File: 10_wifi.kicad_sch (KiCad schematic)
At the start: 25 parts, among them J1 Conn_01x03, J16 Conn_01x04, J30 Conn_01x04, J31 TYPE-C-31-M-12, J32 Conn_01x03, J33 EnUSB, U12 TLV62130, U13 FC41D

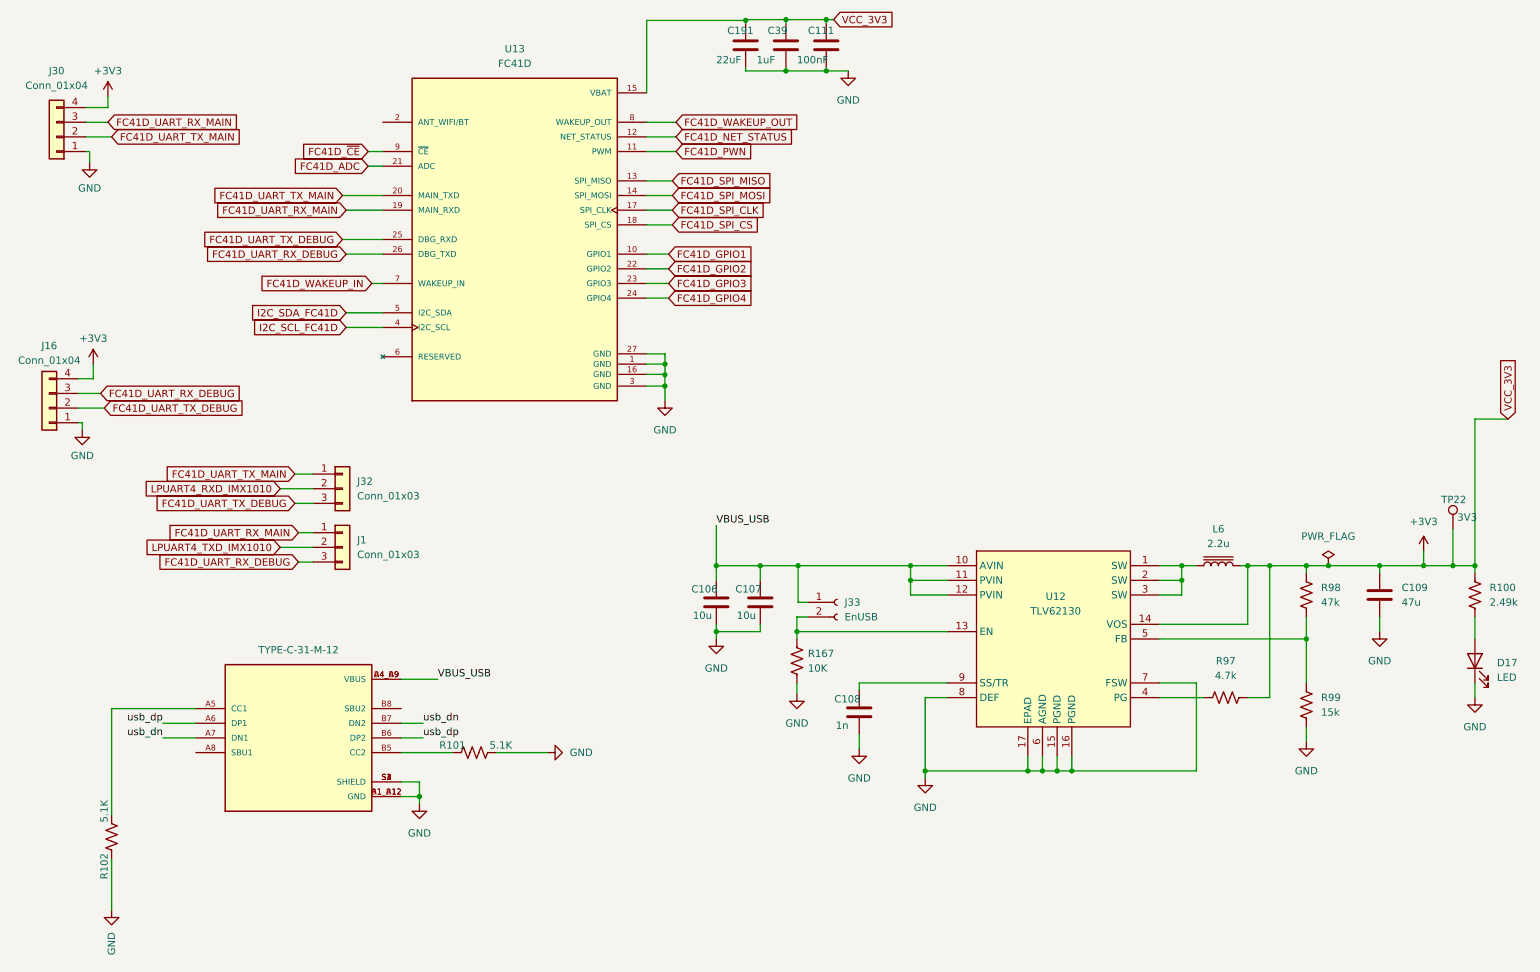
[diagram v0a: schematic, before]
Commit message: add revision to motor
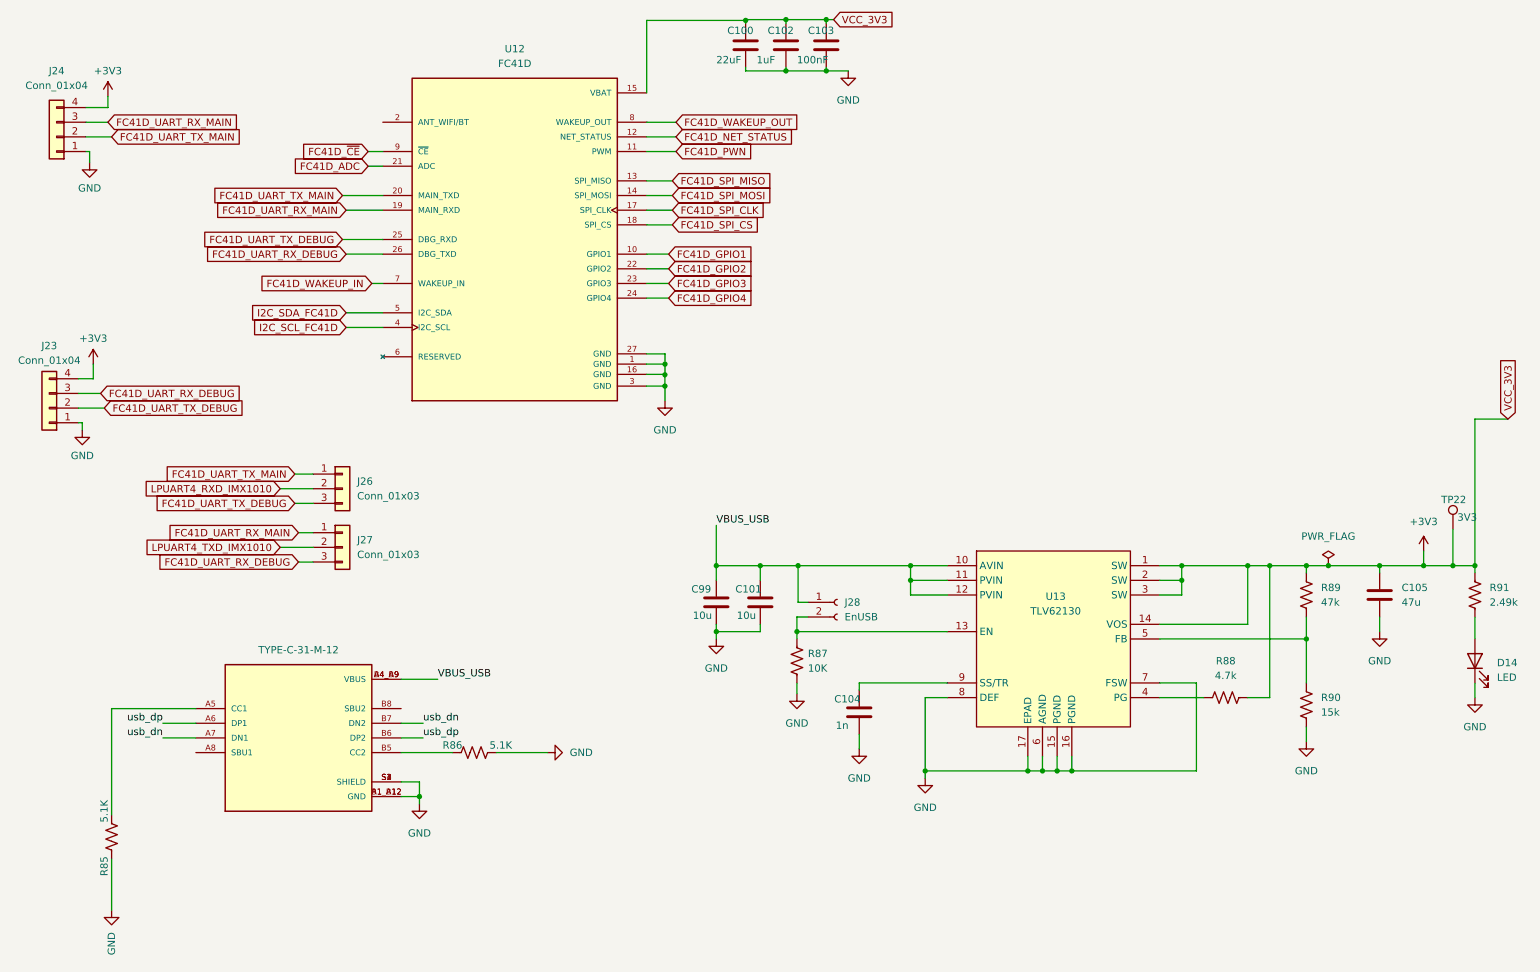
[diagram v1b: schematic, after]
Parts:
- removed L6: 2.2u, Inductor_SMD:L_APV_APH0620, symbol Device:L_Iron
- renumbered C191 to C100, C107 to C101, C39 to C102, C111 to C103, C108 to C104, C109 to C105, C106 to C99, D17 to D14, J16 to J23, J30 to J24, J31 to J25, J32 to J26, J1 to J27, J33 to J28, R102 to R85, R101 to R86, R167 to R87, R97 to R88, R98 to R89, R99 to R90, R100 to R91, U13 to U12, U12 to U13
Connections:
- net +3V3: now also U13.1 (SW), U13.2 (SW), U13.3 (SW)

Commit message: del some
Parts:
- renumbered J23 to J24, J24 to J25, J25 to J26, J26 to J27, J27 to J28, J28 to J29
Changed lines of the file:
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@@
 		(dnp no)
 		(fields_autoplaced yes)
-		(property "Reference" "J26"
+		(property "Reference" "J27"
 			(at 74.295 104.1399 0)
 			(effects
@@
 			(project ""
 				(path "/0db193be-516d-4409-bb62-b8733a9e8874/1395fa6c-ef59-41cc-a4ce-0528bf6ec8b4"
-					(reference "J26")
+					(reference "J27")
 					(unit 1)
 				)
@@
 		(dnp no)
 		(fields_autoplaced yes)
-		(property "Reference" "J28"
+		(property "Reference" "J29"
 			(at 158.75 125.0949 0)
 			(effects
@@
 			(project ""
 				(path "/0db193be-516d-4409-bb62-b8733a9e8874/1395fa6c-ef59-41cc-a4ce-0528bf6ec8b4"
-					(reference "J28")
+					(reference "J29")
 					(unit 1)
 				)
@@
 		(dnp no)
 		(fields_autoplaced yes)
-		(property "Reference" "J25"
+		(property "Reference" "J26"
 			(at 64.135 130.81 0)
 			(effects
@@
 			(project ""
 				(path "/0db193be-516d-4409-bb62-b8733a9e8874/1395fa6c-ef59-41cc-a4ce-0528bf6ec8b4"
-					(reference "J25")
+					(reference "J26")
 					(unit 1)
 				)
@@
 		(dnp no)
 		(fields_autoplaced yes)
-		(property "Reference" "J24"
+		(property "Reference" "J25"
 			(at 22.225 33.02 0)
 			(effects
@@
 			(project ""
 				(path "/0db193be-516d-4409-bb62-b8733a9e8874/1395fa6c-ef59-41cc-a4ce-0528bf6ec8b4"
-					(reference "J24")
+					(reference "J25")
 					(unit 1)
 				)
@@
 		(dnp no)
 		(fields_autoplaced yes)
-		(property "Reference" "J27"
+		(property "Reference" "J28"
 			(at 74.295 114.2999 0)
 			(effects
@@
 			(project "qiot"
 				(path "/0db193be-516d-4409-bb62-b8733a9e8874/1395fa6c-ef59-41cc-a4ce-0528bf6ec8b4"
-					(reference "J27")
+					(reference "J28")
 					(unit 1)
 				)
@@
 		(dnp no)
 		(fields_autoplaced yes)
-		(property "Reference" "J23"
+		(property "Reference" "J24"
 			(at 20.955 80.645 0)
 			(effects
@@
 			(project "qiot"
 				(path "/0db193be-516d-4409-bb62-b8733a9e8874/1395fa6c-ef59-41cc-a4ce-0528bf6ec8b4"
-					(reference "J23")
+					(reference "J24")
 					(unit 1)
 				)

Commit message: dad
da
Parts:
- C100: footprint Resistor_SMD:R_0603_1608Metric -> Capacitor_SMD:C_0603_1608Metric; Manufacturer_Part_Number (none) -> CL10A226MQ8NRNC
- C101, C99: value 10u -> 10uF; Manufacturer_Part_Number (none) -> CS1608X5R106M160NRB
- C102: Manufacturer_Part_Number (none) -> CL05A105KO5NNNC
- C103: Manufacturer_Part_Number (none) -> CS1005X7R104K500NR
- C104: value 1n -> 1nF; Manufacturer_Part_Number (none) -> TCC0402X7R102M500AT
- C105: value 47u -> 47uF; Manufacturer_Part_Number (none) -> 0603X476M6R3NT
- D14: Manufacturer_Part_Number (none) -> C6210741
- J24, J25, J27, J28, J29, TP22: now not fitted
- J26: Manufacturer_Part_Number (none) -> TYPE-C-31-M-12
- R85, R86: Manufacturer_Part_Number (none) -> RC0402FR-075K1L
- R87: Manufacturer_Part_Number (none) -> RC0402FR-0710KL
- R88: value 4.7k -> 4.7K; Manufacturer_Part_Number (none) -> RC0402FR-074K7L
- R89: value 47k -> 47K; Manufacturer_Part_Number (none) -> RC0402FR-0747KL
- R90: value 15k -> 15K; Manufacturer_Part_Number (none) -> 0402WGF1502TCE
- R91: value 2.49k -> 2.49K; Manufacturer_Part_Number (none) -> RTT022491FTH
- U12: Manufacturer_Part_Number (none) -> FC41D
- U13: Manufacturer_Part_Number (none) -> TLV62130RGTR

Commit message: gema
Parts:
- added L8: 2.2uH, symbol Device:L
- C100:  LCSC Part # (none) -> C59461
- C101, C99:  LCSC Part # (none) -> C194427; Manufacturer_Part_Number CS1608X5R106M160NRB -> GRM188R6YA106MA73D
- C102:  LCSC Part # (none) -> C29266
- C103:  LCSC Part # (none) -> C77020; Manufacturer_Part_Number CS1005X7R104K500NR -> GRM155R71H104KE14D
- C104:  LCSC Part # (none) -> C696907
- C105:  LCSC Part # (none) -> C140782; Manufacturer_Part_Number 0603X476M6R3NT -> GRM188R60J476ME15D
- D14:  LCSC Part # (none) -> C6210741
- J26:  LCSC Part # (none) -> C165948
- R85, R86:  LCSC Part # (none) -> C105872
- R87:  LCSC Part # (none) -> C60490
- R88:  LCSC Part # (none) -> C105871
- R89:  LCSC Part # (none) -> C93943
- R90:  LCSC Part # (none) -> C25756
- R91:  LCSC Part # (none) -> C102924
- U12:  LCSC Part # (none) -> FC41D
- U13:  LCSC Part # (none) -> C122479
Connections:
- net +3V3: now also L8.2; no longer U13.1 (SW), U13.2 (SW), U13.3 (SW)
- new net: L8.1, U13.1 (SW), U13.2 (SW), U13.3 (SW)
